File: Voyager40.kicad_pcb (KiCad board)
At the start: 2 copper layers, 244.5 x 76.2 mm, 192 parts, among them Q1 2N7002, SW1 5.2x5.2mm, U1 ATmega32U2-AU, U2 PRTR5V0U2X, Y1 16Mhz

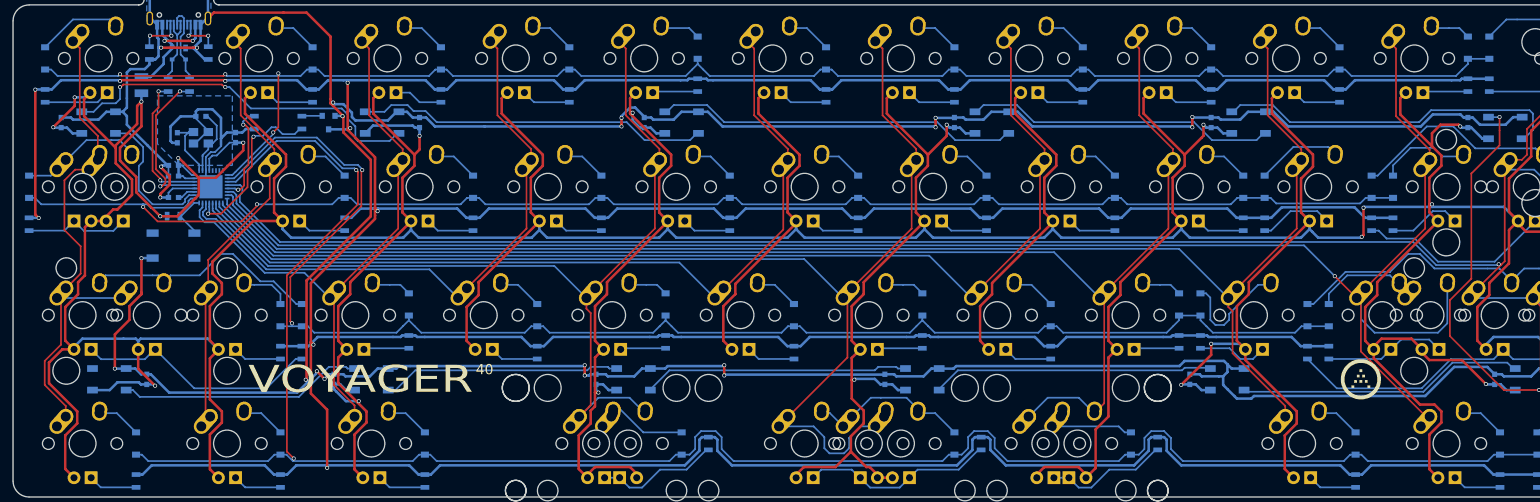
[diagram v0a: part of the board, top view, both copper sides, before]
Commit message: Initial STM32F072CB replacement
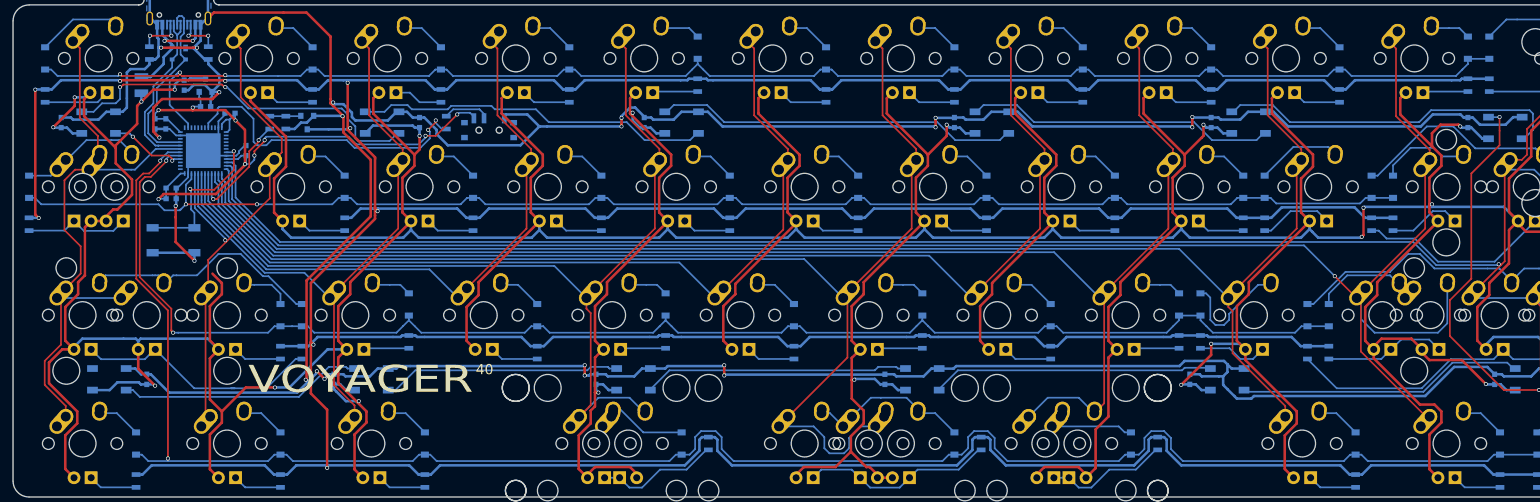
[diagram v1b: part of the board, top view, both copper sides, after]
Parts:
- removed C2: 10uF, Capacitors_SMD:C_0603
- removed C3, C4: 0.1uF, Capacitors_SMD:C_0603
- removed C6: 1uF, Capacitors_SMD:C_0603
- removed C7, C8: 22pF, Capacitors_SMD:C_0603
- removed G***: LOGO, locallib:ai-ring-6mm
- removed G***: LOGO, locallib:ai-4.8-ring
- removed R67, R68: 22, Resistors_SMD:R_0805
- removed R70: 10k, Resistors_SMD:R_0805
- removed R71: 1k, Resistors_SMD:R_0805
- removed SW1: 5.2x5.2mm, random-keyboard-parts:SKQGADE010
- removed U1: ATmega32U2-AU, Housings_DFN_QFN:QFN-32-1EP_5x5mm_Pitch0.5mm
- removed Y1: 16Mhz, Crystals:Crystal_SMD_3225-4pin_3.2x2.5mm
- added C19: 0.1uF, Capacitors_SMD:C_0603, B.Cu at (58.4, 58.9)
- added C20: 0.1uF, Capacitors_SMD:C_0603, B.Cu at (57.6, 49.4)
- added C21: 0.1uF, Capacitors_SMD:C_0603, B.Cu at (67.1, 47.8)
- added C22: 0.1uF, Capacitors_SMD:C_0603, B.Cu at (69.5, 53.4)
- added C23: 4.7uF, Capacitors_SMD:C_0603, B.Cu at (56.0, 49.4)
- added C24: 4.7uF, Capacitors_SMD:C_0603, B.Cu at (58.4, 60.5)
- added C25: 1uF, Capacitors_SMD:C_0603, B.Cu at (60.3, 43.7)
- added C26: 1uF, Capacitors_SMD:C_0603, B.Cu at (63.5, 46.8)
- added R2: 10k, Resistors_SMD:R_0805, B.Cu at (99.2, 49.2)
- added R3: 5.1k, Resistors_SMD:R_0805, B.Cu at (75.4, 49.2)
- added SW2: SW_Push, Buttons_Switches_SMD:SW_SPST_SKQG, B.Cu at (58.7, 66.7)
- added SW3: SW_SPDT, Buttons_Switches_SMD:SW_SPDT_PCM12, B.Cu at (105.6, 50.0)
- added U3: STM32F072CBUx, Housings_DFN_QFN:QFN-48-1EP_7x7mm_Pitch0.5mm, B.Cu at (63.2, 53.4)
- added U4: MCP1700-3002E_SOT23, TO_SOT_Packages_SMD:SOT-23, B.Cu at (63.5, 43.7)
- R69: value 1k -> 100
- moved R69 4.76 mm to (73.0, 49.2)
- moved Q1 3.17 mm to (78.6, 49.2)
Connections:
- U2 pad 2: Net-(R68-Pad2) -> D+
- U2 pad 3: Net-(R67-Pad2) -> D-
- USB1 pad 5: Net-(R67-Pad2) -> D-
- USB1 pad 6: Net-(R68-Pad2) -> D+
- USB1 pad 7: Net-(R67-Pad2) -> D-
- USB1 pad 8: Net-(R68-Pad2) -> D+
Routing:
- net +3V3: track 0.00 -> 101.2 mm, vias 0 -> 9
- net Net-(R2-Pad1): track 0.00 -> 46.3 mm, vias 0 -> 2
- net +5V: track 1291.5 -> 1248.7 mm, vias 21 -> 20
- net GND: track 652.9 -> 679.1 mm
- net Net-(SW2-Pad2): track 0.00 -> 24.0 mm, vias 0 -> 2
- net ROW3: track 299.6 -> 280.1 mm
- net Net-(R71-Pad2): track 15.1 -> 0.00 mm, vias 2 -> 0
- net COL0: track 75.0 -> 89.8 mm
- net COL1: track 61.8 -> 74.8 mm, vias 0 -> 1
- net Net-(R68-Pad2): track 12.0 -> 0.00 mm
- net Net-(R67-Pad2): track 10.5 -> 0.00 mm
- net Net-(C8-Pad1): track 10.1 -> 0.00 mm
- net RGBLED: track 21.6 -> 11.6 mm, vias 0 -> 2
- net Net-(C7-Pad1): track 9.94 -> 0.00 mm
- net ROW0: track 244.2 -> 235.6 mm, vias 4 -> 3
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
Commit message: Produce new gerbers
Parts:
- added G***: LOGO, locallib:ai-4.8-ring, B.Cu at (92.1, 68.3)
- moved C26 0.79 mm to (62.7, 46.8)
- moved C21 0.19 mm to (67.3, 47.8)
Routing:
- net +5V: track 1248.7 -> 1241.1 mm, vias 20 -> 19
- net COL7: track 163.4 -> 162.7 mm
- net COL11: track 321.3 -> 320.6 mm
- net .-COL: track 266.0 -> 265.2 mm
- net COL8: track 213.6 -> 212.9 mm
- net COL6: track 188.0 -> 187.3 mm
- net COL9: track 222.0 -> 221.2 mm
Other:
- board text added: "Voyager40 PCB Rev 2.0 20190217"
- board text removed: "Voyager40 PCB Rev 1.0 20190203"

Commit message: Progress save
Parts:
- moved D16 1.59 mm to (39.7, 38.1)
- moved R16 1.59 mm to (39.7, 43.7)
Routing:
- net LEDGND: track 874.2 -> 875.4 mm
- net ROW0: track 235.6 -> 236.3 mm
- net Net-(K_TAB1-Pad4): track 9.80 -> 10.5 mm
- net Net-(D16-Pad2): track 12.9 -> 12.3 mm

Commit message: Reroute
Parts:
- moved C12 8.87 mm to (258.8, 45.2), turned to 180 degrees
- moved D1 1.59 mm to (234.2, 95.2)
- moved D59 1.59 mm to (53.2, 95.2)
- moved D60 1.59 mm to (74.6, 95.2)
- moved D63 1.59 mm to (255.6, 95.2)
- moved D64 1.59 mm to (261.1, 95.2)
- moved D67 1.59 mm to (96.0, 95.2)
- moved R31 1.59 mm to (37.3, 62.7)
- moved R32 1.59 mm to (84.1, 62.7)
- moved R33 1.59 mm to (103.2, 62.7)
- moved R34 1.59 mm to (122.2, 62.7)
- moved R35 1.59 mm to (141.3, 62.7)
- moved R36 1.59 mm to (160.3, 62.7)
- moved R37 1.59 mm to (179.4, 62.7)
- moved R38 1.59 mm to (198.4, 62.7)
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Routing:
- net GND: track 679.4 -> 704.9 mm, vias 21 -> 17
- net Net-(RGB11-Pad2): track 55.2 -> 80.1 mm
- net LEDGND: track 875.4 -> 850.8 mm
- net ROW1: track 215.5 -> 226.2 mm, vias 2 -> 3
- net ROW0: track 236.3 -> 246.6 mm
- net Net-(D55-Pad2): track 48.6 -> 56.7 mm, vias 0 -> 2
- net ROW3: track 280.1 -> 288.0 mm, vias 2 -> 4
- net Net-(RGB4-Pad2): track 41.8 -> 48.3 mm
- net Net-(R2-Pad1): track 46.3 -> 40.9 mm, vias 2 -> 0
- net RGBLED: track 11.6 -> 16.8 mm
- net Net-(RGB1-Pad2): track 55.2 -> 50.3 mm
- net Net-(RGB11-Pad4): track 51.7 -> 47.2 mm
- net ROW2: track 216.9 -> 221.3 mm, vias 2 -> 4
- net .-COL: track 265.2 -> 261.5 mm, vias 1 -> 2
- net .-ROW: track 16.0 -> 19.6 mm
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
